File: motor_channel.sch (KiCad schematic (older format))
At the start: 18 parts, among them U7 PWD13F60, U8 INA181AX-sternie

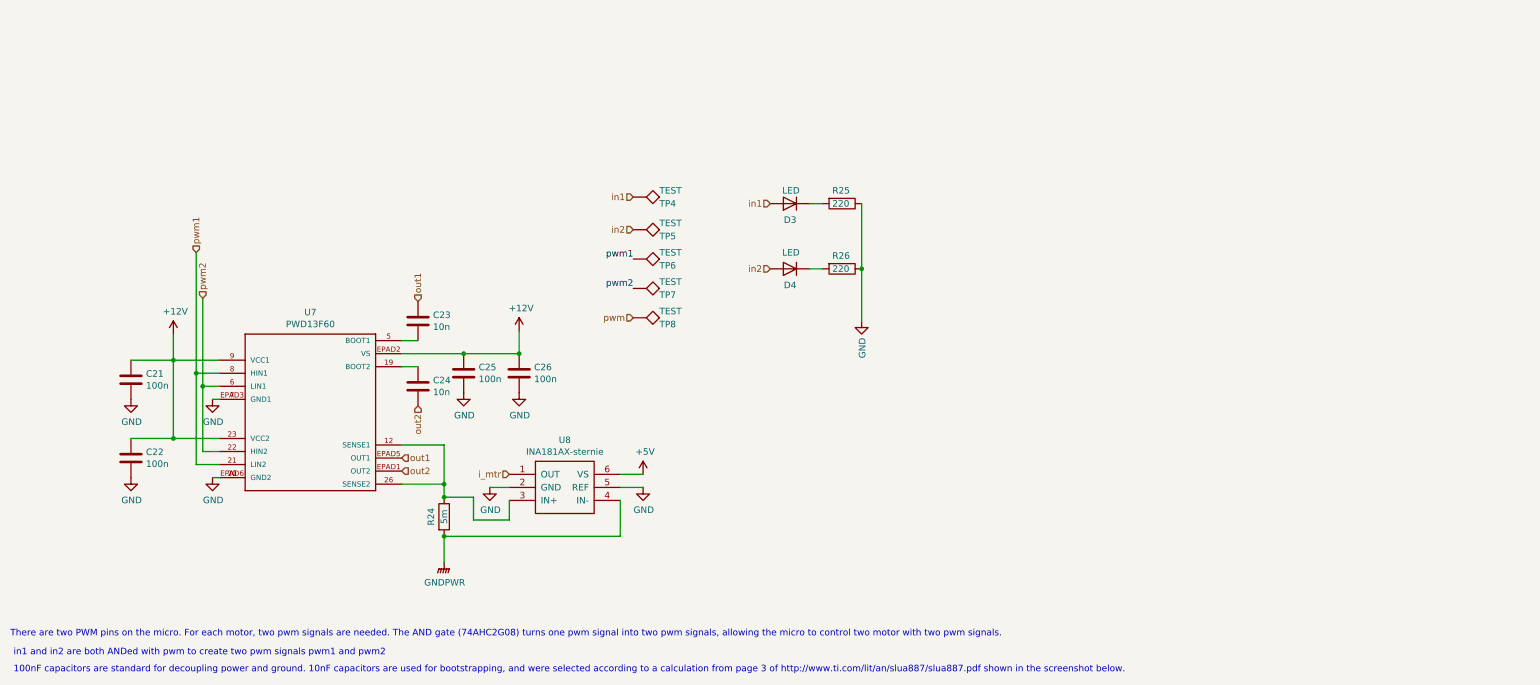
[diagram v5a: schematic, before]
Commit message: Motor Channel Cleanup
Removed some leftover labels in the motor channel after removal of the AND gate. Renumbering.
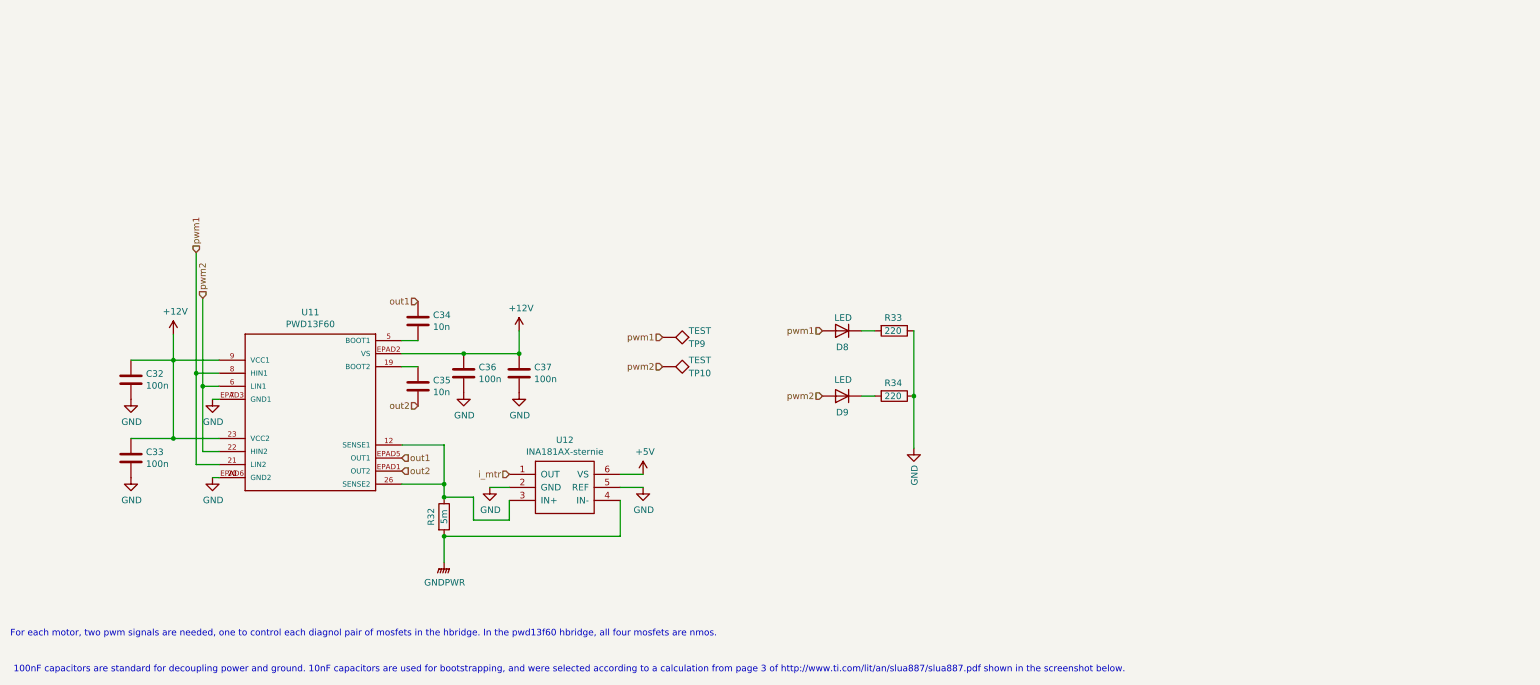
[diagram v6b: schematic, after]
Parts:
- removed TP4, TP5, TP8: TEST, symbol bangbang_rev1-rescue:TEST-Engine_Controller-cache
- renumbered C21 to C32, C22 to C33, C23 to C34, C24 to C35, C25 to C36, C26 to C37, D3 to D8, D4 to D9, R24 to R32, R25 to R33, R26 to R34, TP7 to TP10, TP6 to TP9, U7 to U11, U8 to U12
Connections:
- net in1 is gone; now on net pwm1: D8.2 (A)
- net in2 is gone; now on net pwm2: D9.2 (A)
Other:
- note added: "For each motor, two pwm signals are needed, one to control each diagnol pair of mosfets in the hbridge. In the pwd13f60 hbridge, all four mosfets are nmos."
- note removed: "There are two PWM pins on the micro. For each motor, two pwm signals are needed. The AND gate (74AHC2G08) turns one pwm signal into two pwm signals, allowing the micro to control two motor with two pwm signals."
- note removed: "in1 and in2 are both ANDed with pwm to create two pwm signals pwm1 and pwm2\n\n"
- moved on the sheet: D8, D9, R33, R34, TP10, TP9
